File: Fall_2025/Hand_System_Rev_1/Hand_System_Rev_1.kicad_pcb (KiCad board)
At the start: 2 copper layers, 27 parts, among them J1 Barrel_Jack, M1 Motor_Servo, M2 Motor_Servo, M3 Motor_Servo, M4 Motor_Servo, M5 Motor_Servo, M6 Motor_Servo, M7 Stepper_Motor, U1 ESP32-DEVKITC-32UE, U2 LM2596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

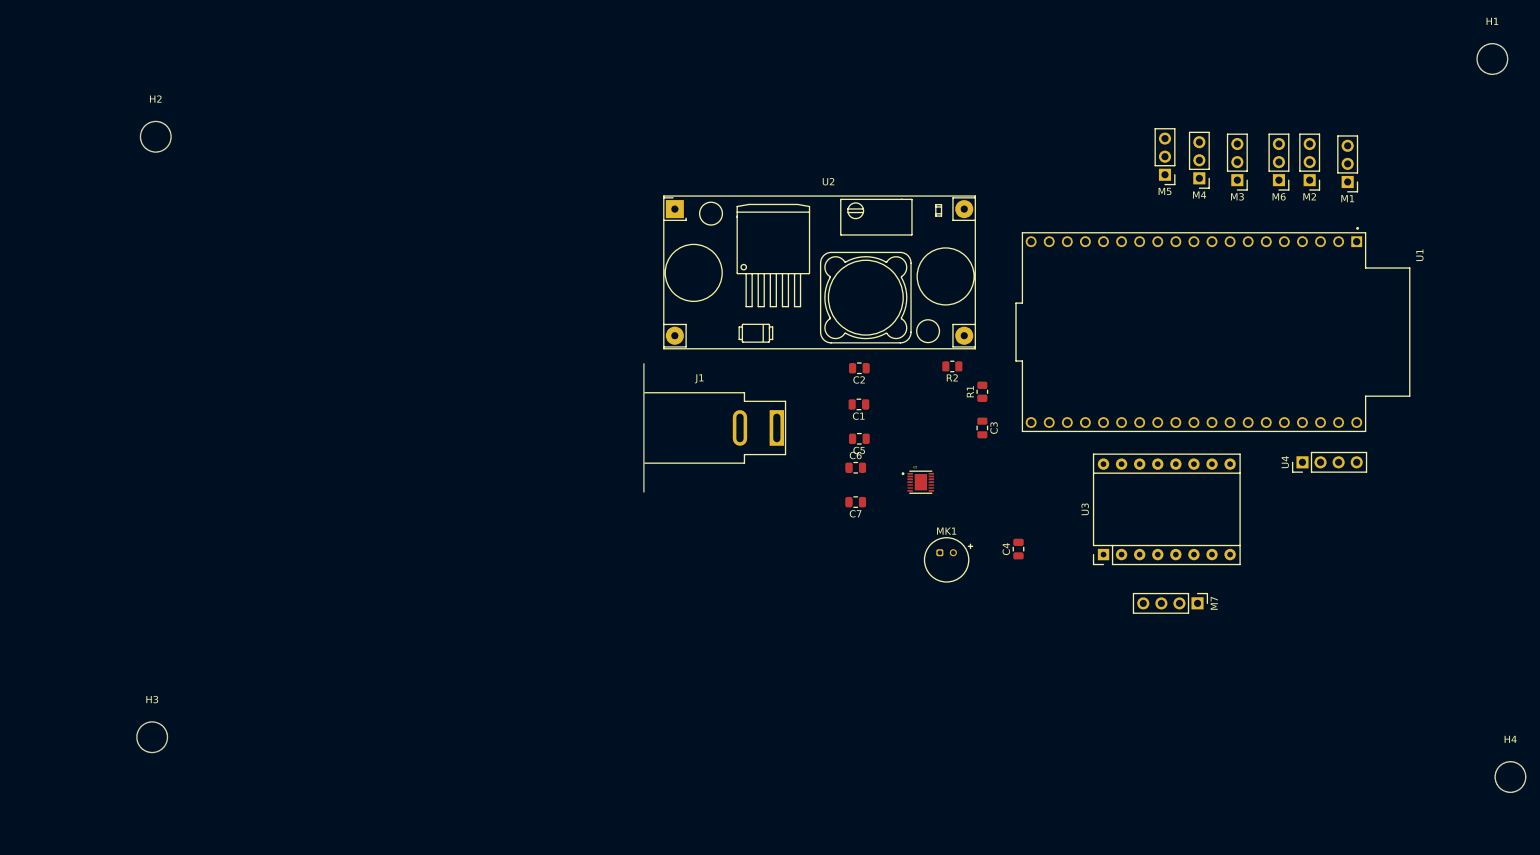
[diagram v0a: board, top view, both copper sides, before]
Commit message: Finalized the pcb design
Included microphone and other modules.

Successfully got gerber files, drill files, and bom
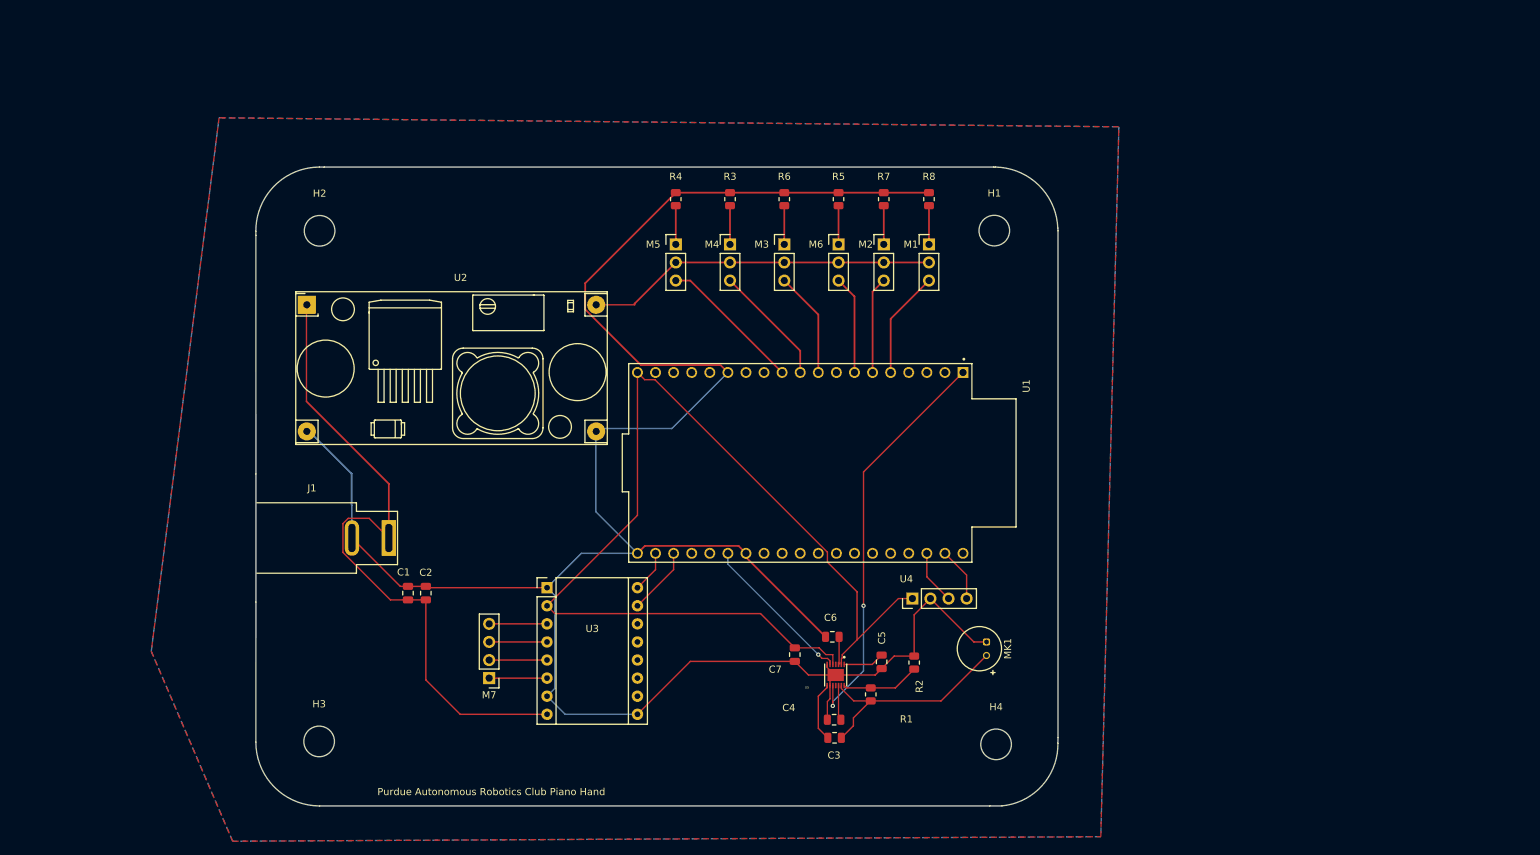
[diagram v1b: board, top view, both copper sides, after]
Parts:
- added R3: 1K, Resistor_SMD:R_0805_2012Metric, F.Cu at (159.4, 51.4)
- added R4: 1K, Resistor_SMD:R_0805_2012Metric, F.Cu at (151.8, 51.4)
- added R5: 1K, Resistor_SMD:R_0805_2012Metric, F.Cu at (174.6, 51.4)
- added R6: 1K, Resistor_SMD:R_0805_2012Metric, F.Cu at (167.0, 51.4)
- added R7: 1K, Resistor_SMD:R_0805_2012Metric, F.Cu at (181.0, 51.4)
- added R8: 1K, Resistor_SMD:R_0805_2012Metric, F.Cu at (187.3, 51.4)
- moved M7 100.0 mm to (125.6, 118.7), turned to 180 degrees
- moved U3 78.3 mm to (133.7, 106.0), turned to 0 degrees
- moved H1 74.0 mm to (196.5, 55.9)
- moved H4 72.4 mm to (196.8, 128.0)
- moved M5 69.4 mm to (151.8, 57.8), turned to 0 degrees
- moved C1 68.6 mm to (114.2, 106.8), turned to 90 degrees
- moved C2 68.6 mm to (116.7, 106.8), turned to 90 degrees
- moved M4 66.6 mm to (159.4, 57.8), turned to 0 degrees
- moved M3 64.3 mm to (167.0, 57.8), turned to 0 degrees
- moved M6 62.5 mm to (174.6, 57.8), turned to 0 degrees
- moved M2 60.5 mm to (181.0, 57.8), turned to 0 degrees
- moved M1 59.5 mm to (187.3, 57.8), turned to 0 degrees
- moved U1 58.3 mm to (169.3, 88.5)
- moved U4 58.0 mm to (185.0, 107.5)
- moved J1 56.6 mm to (111.5, 99.0)
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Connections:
- C7 pad 1: 3.3V -> 5V
- M1 pad 1: /THUMB_1 -> Net-(M1--)
- M1 pad 3: GND -> /THUMB_1
- M2 pad 1: /THUMB_2 -> Net-(M2--)
- M2 pad 3: GND -> /THUMB_2
- M3 pad 1: /INDEX -> Net-(M3--)
- M3 pad 3: GND -> /INDEX
- M4 pad 1: /MIDDLE -> Net-(M4--)
- M4 pad 3: GND -> /MIDDLE
- M5 pad 1: /RING -> Net-(M5--)
- M5 pad 3: GND -> /RING
- M6 pad 1: /PINKIE -> Net-(M6--)
- M6 pad 3: GND -> /PINKIE
- U1 pad 18: /MP_OUT -> unconnected-(U1-CMD-Pad18)
- U1 pad 2: 3.3V -> unconnected-(U1-EN-Pad2)
- U1 pad 25: unconnected-(U1-21-Pad25) -> /MP_OUT
- U3 pad 2: 3.3V -> 5V
- U4 pad 1: 3.3V -> 5V
- U5 pad 2: 3.3V -> 5V
- U5 pad 5: 3.3V -> 5V
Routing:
- net GND: track 0.00 -> 320.7 mm
- net 5V: track 0.00 -> 148.1 mm
- net 12V: track 0.00 -> 94.5 mm
- net 3.3V: track 0.00 -> 57.3 mm, vias 0 -> 2
- net 7.2V: track 0.00 -> 49.3 mm
- net Net-(MK1-+): track 0.00 -> 31.1 mm
- net /MP_OUT: track 0.00 -> 22.0 mm, vias 0 -> 1
- net /RING: track 0.00 -> 20.3 mm
- net /MIDDLE: track 0.00 -> 17.0 mm
- net /THUMB_1: track 0.00 -> 15.1 mm
- net /INDEX: track 0.00 -> 14.9 mm
- net /PINKIE: track 0.00 -> 13.8 mm
- net /THUMB_2: track 0.00 -> 13.6 mm
- net Net-(U5-TH): track 0.00 -> 11.0 mm
- net /STEP_PIN: track 0.00 -> 9.47 mm
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- added copper zone on B.Cu, net GND
- added copper zone on F.Cu, net GND
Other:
- board outline added: 112.7 x 89.7 mm
- board text added: "Purdue Autonomous Robotics Club Piano Hand"

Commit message: added more stuff
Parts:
- removed C3: 0.1uF, Capacitor_SMD:C_0805_2012Metric
- removed C4: 0.47uF, Capacitor_SMD:C_0805_2012Metric
- removed C5: 470nF, Capacitor_SMD:C_0805_2012Metric
- removed C6: 2.2uF, Capacitor_SMD:C_0805_2012Metric
- removed C7: 1uF, Capacitor_SMD:C_0805_2012Metric
- removed MK1: Microphone, Sensor_Audio:POM-2244P-C3310-2-R
- added M10: Motor_Servo, Connector_PinHeader_2.54mm:PinHeader_1x03_P2.54mm_Vertical, F.Cu at (215.3, 117.9)
- added M11: Motor_Servo, Connector_PinHeader_2.54mm:PinHeader_1x03_P2.54mm_Vertical, F.Cu at (227.5, 117.9)
- added M8: Motor_Servo, Connector_PinHeader_2.54mm:PinHeader_1x03_P2.54mm_Vertical, F.Cu at (190.1, 117.9)
- added M9: Motor_Servo, Connector_PinHeader_2.54mm:PinHeader_1x03_P2.54mm_Vertical, F.Cu at (202.8, 117.9)
- added Q1: IRF6623, Package_DirectFET:DirectFET_ST, F.Cu at (173.1, 54.6)
- added Q2: IRF6623, Package_DirectFET:DirectFET_ST, F.Cu at (116.9, 77.7)
- added R10: 1K, Resistor_SMD:R_0805_2012Metric, F.Cu at (202.8, 125.1)
- added R11: 1K, Resistor_SMD:R_0805_2012Metric, F.Cu at (215.3, 125.1)
- added R12: 1K, Resistor_SMD:R_0805_2012Metric, F.Cu at (227.2, 125.1)
- added R13: 1k, Resistor_SMD:R_0805_2012Metric, F.Cu at (170.7, 115.6)
- added R14: 10k, Resistor_SMD:R_0805_2012Metric, F.Cu at (110.6, 77.5)
- added R15: 1k, Resistor_SMD:R_0805_2012Metric, F.Cu at (125.5, 78.0)
- added R16: 1k, Resistor_SMD:R_0805_2012Metric, F.Cu at (133.8, 105.7)
- added R9: 1K, Resistor_SMD:R_0805_2012Metric, F.Cu at (190.1, 125.1)
- R1: value 150k -> 10k
- R2: value 100k -> 1k
- U5: value MAX9814ETD_T -> LM2596; footprint MAX9814ETD_T:SON40P300X300X80-15N -> PCB_Components:LM2596
- moved H4 131.9 mm to (65.2, 136.1)
- moved H3 130.0 mm to (231.5, 133.6)
- moved R4 101.0 mm to (220.9, 125.1), turned to 90 degrees
- moved R5 94.0 mm to (233.0, 125.1), turned to 90 degrees
- moved M5 91.6 mm to (220.9, 117.9), turned to 180 degrees
- moved U5 91.3 mm to (117.7, 46.5), turned to 0 degrees
- moved R3 88.5 mm to (208.4, 125.1), turned to 90 degrees
- moved M6 83.8 mm to (233.0, 117.9), turned to 180 degrees
- moved R6 79.1 mm to (195.7, 125.1), turned to 90 degrees
- moved M4 77.5 mm to (208.4, 117.9), turned to 180 degrees
- moved R1 75.2 mm to (171.0, 46.2), turned to 0 degrees
- moved R8 74.2 mm to (178.2, 125.1), turned to 90 degrees
- moved R7 73.7 mm to (183.5, 125.1), turned to 90 degrees
- moved M3 66.6 mm to (195.7, 117.9), turned to 180 degrees
- moved R2 61.8 mm to (181.1, 54.9), turned to 180 degrees
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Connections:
- C1 pad 1: 12V -> 15V
- C2 pad 1: 12V -> STP_P
- J1 pad 1: 12V -> 15V
- M1 pad 2: 7.2V -> MOTOR_P
- M2 pad 2: 7.2V -> MOTOR_P
- M3 pad 2: 7.2V -> MOTOR_P
- M3 pad 3: /INDEX -> /INDEX_2
- M4 pad 2: 7.2V -> MOTOR_P
- M4 pad 3: /MIDDLE -> /MIDDLE_2
- M5 pad 2: 7.2V -> MOTOR_P
- M5 pad 3: /RING -> /RING_2
- M6 pad 2: 7.2V -> MOTOR_P
- M6 pad 3: /PINKIE -> /PINKIE_2
- R1 pad 1: Net-(MK1-+) -> 7.2V
- R1 pad 2: Net-(U5-TH) -> Net-(Q1-D)
- R2 pad 1: Net-(U5-TH) -> /SERVO_VG
- R2 pad 2: GND -> Net-(Q1-G)
- U1 pad 10: /MIDDLE -> unconnected-(U1-26-Pad10)
- U1 pad 11: /RING -> unconnected-(U1-27-Pad11)
- U1 pad 12: unconnected-(U1-14-Pad12) -> /DT
- U1 pad 13: unconnected-(U1-12-Pad13) -> /CW
- U1 pad 15: unconnected-(U1-13-Pad15) -> /STP_VG
- U1 pad 16: unconnected-(U1-D2-Pad16) -> /SERVO_VG
- U1 pad 23: unconnected-(U1-TX-Pad23) -> /THUMB_1
- U1 pad 24: unconnected-(U1-RX-Pad24) -> /THUMB_2
- U1 pad 25: /MP_OUT -> /INDEX_1
- U1 pad 27: unconnected-(U1-19-Pad27) -> /INDEX_2
- U1 pad 28: unconnected-(U1-18-Pad28) -> /MIDDLE_1
- U1 pad 29: unconnected-(U1-5-Pad29) -> /MIDDLE_2
- U1 pad 30: unconnected-(U1-17-Pad30) -> /RING_1
- U1 pad 31: unconnected-(U1-16-Pad31) -> /RING_2
- U1 pad 32: unconnected-(U1-4-Pad32) -> /PINKIE_1
- U1 pad 33: unconnected-(U1-0-Pad33) -> /PINKIE_2
- U1 pad 36: /CW -> unconnected-(U1-D1-Pad36)
- U1 pad 37: /DT -> unconnected-(U1-D0-Pad37)
- U1 pad 5: /THUMB_1 -> unconnected-(U1-34-Pad5)
- U1 pad 6: /THUMB_2 -> unconnected-(U1-35-Pad6)
- U1 pad 7: /PINKIE -> unconnected-(U1-32-Pad7)
- U1 pad 9: /INDEX -> unconnected-(U1-25-Pad9)
- U2 pad 1: 12V -> 15V
- U2 pad 4: 7.2V -> 12V
- U3 pad 8: 12V -> STP_P
- U5 pad 1: Net-(U5-CT) -> 12V
- U5 pad 2: 5V -> GND
- U5 pad 3: Net-(U5-CG) -> GND
- U5 pad 4: (no net) -> 7.2V
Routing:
- net /STP_VG: track 0.00 -> 91.1 mm
- net Net-(Q1-S): track 0.00 -> 76.4 mm
- net GND: track 320.7 -> 386.5 mm
- net 5V: track 148.1 -> 86.0 mm
- net MOTOR_P: track 0.00 -> 61.6 mm
- net 3.3V: track 57.3 -> 0.00 mm, vias 2 -> 0
- net 12V: track 94.5 -> 41.9 mm
- net 15V: track 0.00 -> 51.0 mm
- net STP_P: track 0.00 -> 45.6 mm
- net 7.2V: track 49.3 -> 11.8 mm
- net Net-(Q2-S): track 0.00 -> 34.8 mm
- net /DIR_PIN: track 5.88 -> 39.9 mm
- net /STEP_PIN: track 9.47 -> 41.6 mm
- net Net-(MK1-+): track 31.1 -> 0.00 mm
- net Net-(Q1-D): track 0.00 -> 28.2 mm
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- removed copper zone on B.Cu, net GND
- removed copper zone on F.Cu, net GND
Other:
- board outline removed
- copper layers 2 -> 4
- board text removed: "Purdue Autonomous Robotics Club Piano Hand"

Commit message: more stuff for organizing into spring 2026
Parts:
- removed M10, M11, M8, M9: Motor_Servo, Connector_PinHeader_2.54mm:PinHeader_1x03_P2.54mm_Vertical
- removed Q1, Q2: IRF6623, Package_DirectFET:DirectFET_ST
- removed R10, R11, R12, R9: 1K, Resistor_SMD:R_0805_2012Metric
- removed R13, R15, R16: 1k, Resistor_SMD:R_0805_2012Metric
- removed R14: 10k, Resistor_SMD:R_0805_2012Metric
- added C3: 0.1uF, Capacitor_SMD:C_0805_2012Metric, F.Cu at (174.1, 127.1)
- added C4: 0.47uF, Capacitor_SMD:C_0805_2012Metric, F.Cu at (174.0, 124.5)
- added C5: 470nF, Capacitor_SMD:C_0805_2012Metric, F.Cu at (180.7, 116.4)
- added C6: 2.2uF, Capacitor_SMD:C_0805_2012Metric, F.Cu at (173.8, 112.9)
- added C7: 1uF, Capacitor_SMD:C_0805_2012Metric, F.Cu at (168.5, 115.4)
- added MK1: Microphone, Sensor_Audio:POM-2244P-C3310-2-R, F.Cu at (195.4, 113.6)
- R1: value 10k -> 150k
- R2: value 1k -> 100k
- U5: value LM2596 -> MAX9814ETD_T; footprint PCB_Components:LM2596 -> MAX9814ETD_T:SON40P300X300X80-15N
- moved H4 131.9 mm to (196.8, 128.0)
- moved H3 130.0 mm to (101.7, 127.6)
- moved R4 101.0 mm to (151.8, 51.4), turned to -90 degrees
- moved R5 94.0 mm to (174.6, 51.4), turned to -90 degrees
- moved M5 91.6 mm to (151.8, 57.8), turned to 0 degrees
- moved U5 91.3 mm to (174.2, 118.3), turned to -90 degrees
- moved R3 88.5 mm to (159.4, 51.4), turned to -90 degrees
- moved M6 83.8 mm to (174.6, 57.8), turned to 0 degrees
- moved R6 79.1 mm to (167.0, 51.4), turned to -90 degrees
- moved M4 77.5 mm to (159.4, 57.8), turned to 0 degrees
- moved R1 75.2 mm to (179.2, 121.0), turned to 90 degrees
- moved R8 74.2 mm to (187.3, 51.4), turned to -90 degrees
- moved R7 73.7 mm to (181.0, 51.4), turned to -90 degrees
- moved M3 66.6 mm to (167.0, 57.8), turned to 0 degrees
- moved R2 61.8 mm to (185.2, 116.5), turned to 90 degrees
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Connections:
- C1 pad 1: 15V -> 12V
- C2 pad 1: STP_P -> 12V
- J1 pad 1: 15V -> 12V
- M1 pad 2: MOTOR_P -> 7.2V
- M2 pad 2: MOTOR_P -> 7.2V
- M3 pad 2: MOTOR_P -> 7.2V
- M3 pad 3: /INDEX_2 -> /INDEX
- M4 pad 2: MOTOR_P -> 7.2V
- M4 pad 3: /MIDDLE_2 -> /MIDDLE
- M5 pad 2: MOTOR_P -> 7.2V
- M5 pad 3: /RING_2 -> /RING
- M6 pad 2: MOTOR_P -> 7.2V
- M6 pad 3: /PINKIE_2 -> /PINKIE
- R1 pad 1: 7.2V -> Net-(MK1-+)
- R1 pad 2: Net-(Q1-D) -> Net-(U5-TH)
- R2 pad 1: /SERVO_VG -> Net-(U5-TH)
- R2 pad 2: Net-(Q1-G) -> GND
- U1 pad 10: unconnected-(U1-26-Pad10) -> /MIDDLE
- U1 pad 11: unconnected-(U1-27-Pad11) -> /RING
- U1 pad 12: /DT -> unconnected-(U1-14-Pad12)
- U1 pad 13: /CW -> unconnected-(U1-12-Pad13)
- U1 pad 15: /STP_VG -> unconnected-(U1-13-Pad15)
- U1 pad 16: /SERVO_VG -> unconnected-(U1-D2-Pad16)
- U1 pad 23: /THUMB_1 -> unconnected-(U1-TX-Pad23)
- U1 pad 24: /THUMB_2 -> unconnected-(U1-RX-Pad24)
- U1 pad 25: /INDEX_1 -> /MP_OUT
- U1 pad 27: /INDEX_2 -> unconnected-(U1-19-Pad27)
- U1 pad 28: /MIDDLE_1 -> unconnected-(U1-18-Pad28)
- U1 pad 29: /MIDDLE_2 -> unconnected-(U1-5-Pad29)
- U1 pad 30: /RING_1 -> unconnected-(U1-17-Pad30)
- U1 pad 31: /RING_2 -> unconnected-(U1-16-Pad31)
- U1 pad 32: /PINKIE_1 -> unconnected-(U1-4-Pad32)
- U1 pad 33: /PINKIE_2 -> unconnected-(U1-0-Pad33)
- U1 pad 36: unconnected-(U1-D1-Pad36) -> /CW
- U1 pad 37: unconnected-(U1-D0-Pad37) -> /DT
- U1 pad 5: unconnected-(U1-34-Pad5) -> /THUMB_1
- U1 pad 6: unconnected-(U1-35-Pad6) -> /THUMB_2
- U1 pad 7: unconnected-(U1-32-Pad7) -> /PINKIE
- U1 pad 9: unconnected-(U1-25-Pad9) -> /INDEX
- U2 pad 1: 15V -> 12V
- U2 pad 4: 12V -> 7.2V
- U3 pad 8: STP_P -> 12V
- U5 pad 1: 12V -> Net-(U5-CT)
- U5 pad 2: GND -> 5V
- U5 pad 3: GND -> Net-(U5-CG)
- U5 pad 4: 7.2V -> (no net)
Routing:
- net /STP_VG: track 91.1 -> 0.00 mm
- net Net-(Q1-S): track 76.4 -> 0.00 mm
- net GND: track 386.5 -> 320.7 mm
- net 5V: track 86.0 -> 148.1 mm
- net MOTOR_P: track 61.6 -> 0.00 mm
- net 3.3V: track 0.00 -> 57.3 mm, vias 0 -> 2
- net 12V: track 41.9 -> 94.5 mm
- net 15V: track 51.0 -> 0.00 mm
- net STP_P: track 45.6 -> 0.00 mm
- net 7.2V: track 11.8 -> 49.3 mm
- net Net-(Q2-S): track 34.8 -> 0.00 mm
- net /DIR_PIN: track 39.9 -> 5.88 mm
- net /STEP_PIN: track 41.6 -> 9.47 mm
- net Net-(MK1-+): track 0.00 -> 31.1 mm
- net Net-(Q1-D): track 28.2 -> 0.00 mm
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- added copper zone on B.Cu, net GND
- added copper zone on F.Cu, net GND
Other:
- board outline added: 112.7 x 89.7 mm
- copper layers 4 -> 2
- board text added: "Purdue Autonomous Robotics Club Piano Hand"
